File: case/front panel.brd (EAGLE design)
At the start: 165 x 30.1 mm, 3 parts, among them J16 8pin

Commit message: front panel pcb v1.0
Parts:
- added LED2: RGBLED5050, adafruit:RGBLED5050
- added R2, R3, R4: 3.3k, FlashPCB_Resistors:RES-0402
- moved LED1 1.00 mm to (73.0, 4.00)
- moved R1 1.00 mm to (71.9, 3.70)
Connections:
- new net BLUE: J16.8, R2.P$2
- new net BLUE_R: LED2.3, R2.P$1
- new net GREEN: J16.6, R3.P$2
- new net GREEN_R: LED2.1, R3.P$1
- new net RED: J16.4, R4.P$2
- new net RED_R: LED2.2, R4.P$1
- net 5V: now also J16.3, J16.5, J16.7
- net GND: now also LED2.4, LED2.5, LED2.6
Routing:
- net RED: track 0.00 -> 59.1 mm
- net BLUE: track 0.00 -> 54.1 mm
- net GND: track 0.00 -> 50.2 mm
- net GREEN: track 0.00 -> 47.6 mm
- net 5V: track 0.00 -> 23.0 mm
- net RED_R: track 0.00 -> 2.30 mm
- net GREEN_R: track 0.00 -> 2.30 mm
- net BLUE_R: track 0.00 -> 2.30 mm
- net N$1: track 0.00 -> 1.33 mm
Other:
- board text added: "HaasoscopePro v1.0 by DrAndyHaas"
- board text removed: "Haasoscope Pro Power board, v1.2 by Dr. Andy Haas"
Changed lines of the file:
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@@
 <wire x1="161" y1="30.13" x2="4" y2="30.13" width="0" layer="20"/>
 <wire x1="4" y1="30.13" x2="0" y2="26.13" width="0" layer="20" curve="90"/>
-<text x="78.277" y="20.021" size="1.4224" layer="21" font="vector">Haasoscope Pro
-Power board, v1.2
-by Dr. Andy Haas</text>
+<text x="78.277" y="20.021" size="1.778" layer="21" font="vector" ratio="10">HaasoscopePro v1.0
+by DrAndyHaas</text>
 <hole x="4.75" y="26.33" drill="4.5"/>
 <hole x="160.25" y="26.33" drill="4.5"/>
 <hole x="160.25" y="3.8" drill="4.5"/>
 <hole x="4.75" y="3.8" drill="4.5"/>
-<text x="73.428" y="5.711" size="0.8128" layer="21">5V</text>
+<text x="72.428" y="5.711" size="0.8128" layer="21">5V</text>
 <wire x1="108" y1="13" x2="120" y2="13" width="0.1524" layer="20"/>
 <wire x1="120" y1="13" x2="120" y2="8" width="0.1524" layer="20"/>
@@
 <attribute name="PROD_ID" value="CONN-08438" x="77" y="4" size="1.778" layer="27" display="off"/>
 </element>
-<element name="R1" library="FlashPCB_Resistors" package="RES-0402" value="3.3k" x="72.9" y="3.7" smashed="yes" rot="R90"/>
-<element name="LED1" library="adafruit" library_urn="urn:adsk.eagle:library:420" package="CHIP-LED0603" package3d_urn="urn:adsk.eagle:package:6240556/1" value="red" x="74" y="4" smashed="yes"/>
+<element name="R1" library="FlashPCB_Resistors" package="RES-0402" value="3.3k" x="71.9" y="3.7" smashed="yes" rot="R90"/>
+<element name="LED1" library="adafruit" library_urn="urn:adsk.eagle:library:420" package="CHIP-LED0603" package3d_urn="urn:adsk.eagle:package:6240556/1" value="red" x="73" y="4" smashed="yes"/>
+<element name="LED2" library="adafruit" library_urn="urn:adsk.eagle:library:420" package="RGBLED5050" package3d_urn="urn:adsk.eagle:package:6240865/1" value="RGBLED5050" x="39" y="11" smashed="yes" rot="R180">
+<attribute name="LCSC" value="C2827258" x="39" y="11" size="1.778" layer="27" rot="R180" display="off"/>
+<attribute name="NAME" x="40.7" y="8.1" size="1.27" layer="25" font="vector" rot="R180"/>
+</element>
+<element name="R2" library="FlashPCB_Resistors" package="RES-0402" value="3.3k" x="43.8" y="12.7" smashed="yes"/>
+<element name="R3" library="FlashPCB_Resistors" package="RES-0402" value="3.3k" x="43.8" y="9.3" smashed="yes"/>
+<element name="R4" library="FlashPCB_Resistors" package="RES-0402" value="3.3k" x="43.8" y="11" smashed="yes"/>
 </elements>
 <signals>
@@
 <contactref element="R1" pad="P$1"/>
 <contactref element="J16" pad="2"/>
-<wire x1="79.54" y1="4" x2="72.9" y2="3.2" width="0" layer="19" extent="1-1"/>
+<contactref element="LED2" pad="5"/>
+<contactref element="LED2" pad="4"/>
+<contactref element="LED2" pad="6"/>
+<wire x1="72.2952" y1="2.72375" x2="72.47375" y2="2.5452" width="0.3048" layer="1"/>
+<wire x1="71.9" y1="3.2" x2="72.2952" y2="2.8048" width="0.3048" layer="1"/>
+<wire x1="72.2952" y1="2.8048" x2="72.2952" y2="2.72375" width="0.3048" layer="1"/>
+<wire x1="72.47375" y1="2.5452" x2="78.0852" y2="2.5452" width="0.3048" layer="1"/>
+<wire x1="78.0852" y1="2.5452" x2="79.54" y2="4" width="0.3048" layer="1"/>
+<wire x1="37" y1="12.7" x2="37" y2="11" width="0.3048" layer="1"/>
+<wire x1="37" y1="11" x2="37" y2="9.3" width="0.3048" layer="1"/>
+<wire x1="37" y1="9.3" x2="43.7548" y2="2.5452" width="0.3048" layer="1"/>
+<wire x1="43.7548" y1="2.5452" x2="72.47375" y2="2.5452" width="0.3048" layer="1"/>
 </signal>
 <signal name="SW4">
@@
 <contactref element="R1" pad="P$2"/>
 <contactref element="LED1" pad="C"/>
-<wire x1="74" y1="4.75" x2="72.9" y2="4.2" width="0" layer="19" extent="1-1"/>
+<wire x1="73" y1="4.75" x2="72.45" y2="4.2" width="0.3048" layer="1"/>
+<wire x1="72.45" y1="4.2" x2="71.9" y2="4.2" width="0.3048" layer="1"/>
 </signal>
 <signal name="5V">
 <contactref element="LED1" pad="A"/>
 <contactref element="J16" pad="1"/>
-<wire x1="74" y1="3.25" x2="77" y2="4" width="0" layer="19" extent="1-1"/>
+<contactref element="J16" pad="3"/>
+<contactref element="J16" pad="5"/>
+<contactref element="J16" pad="7"/>
+<wire x1="77" y1="4" x2="76.25" y2="3.25" width="0.3048" layer="1"/>
+<wire x1="76.25" y1="3.25" x2="73" y2="3.25" width="0.3048" layer="1"/>
+<wire x1="79.02446875" y1="5.2446" x2="80.05553125" y2="5.2446" width="0.3048" layer="1"/>
+<wire x1="77" y1="4" x2="77.77986875" y2="4" width="0.3048" layer="1"/>
+<wire x1="81.30013125" y1="4" x2="82.08" y2="4" width="0.3048" layer="1"/>
+<wire x1="77.77986875" y1="4" x2="79.02446875" y2="5.2446" width="0.3048" layer="1"/>
+<wire x1="80.05553125" y1="5.2446" x2="81.30013125" y2="4" width="0.3048" layer="1"/>
+<wire x1="84.10446875" y1="2.7554" x2="85.13553125" y2="2.7554" width="0.3048" layer="1"/>
+<wire x1="82.08" y1="4" x2="82.85986875" y2="4" width="0.3048" layer="1"/>
+<wire x1="86.38013125" y1="4" x2="87.16" y2="4" width="0.3048" layer="1"/>
+<wire x1="82.85986875" y1="4" x2="84.10446875" y2="2.7554" width="0.3048" layer="1"/>
+<wire x1="85.13553125" y1="2.7554" x2="86.38013125" y2="4" width="0.3048" layer="1"/>
+<wire x1="88.9950875" y1="2.2982" x2="90.4049125" y2="2.2982" width="0.3048" layer="1"/>
+<wire x1="87.16" y1="4" x2="87.2932875" y2="4" width="0.3048" layer="1"/>
+<wire x1="92.1067125" y1="4" x2="92.24" y2="4" width="0.3048" layer="1"/>
+<wire x1="87.2932875" y1="4" x2="88.9950875" y2="2.2982" width="0.3048" layer="1"/>
+<wire x1="90.4049125" y1="2.2982" x2="92.1067125" y2="4" width="0.3048" layer="1"/>
+</signal>
+<signal name="BLUE">
+<contactref element="J16" pad="8"/>
+<contactref element="R2" pad="P$2"/>
+<wire x1="44.3" y1="12.7" x2="86.08" y2="12.7" width="0.3048" layer="1"/>
+<wire x1="86.08" y1="12.7" x2="94.78" y2="4" width="0.3048" layer="1"/>
+</signal>
+<signal name="GREEN">
+<contactref element="J16" pad="6"/>
+<contactref element="R3" pad="P$2"/>
+<wire x1="89.7" y1="4" x2="84.4" y2="9.3" width="0.3048" layer="1"/>
+<wire x1="84.4" y1="9.3" x2="44.3" y2="9.3" width="0.3048" layer="1"/>
+</signal>
+<signal name="RED">
+<contactref element="J16" pad="4"/>
+<contactref element="R4" pad="P$2"/>
+<wire x1="88.4554" y1="3.48446875" x2="89.18446875" y2="2.7554" width="0.3048" layer="1"/>
+<wire x1="89.18446875" y1="2.7554" x2="90.21553125" y2="2.7554" width="0.3048" layer="1"/>
+<wire x1="90.21553125" y1="2.7554" x2="90.9446" y2="3.48446875" width="0.3048" layer="1"/>
+<wire x1="90.9446" y1="3.48446875" x2="90.9446" y2="4.51553125" width="0.3048" layer="1"/>
+<wire x1="90.9446" y1="4.51553125" x2="90.21553125" y2="5.2446" width="0.3048" layer="1"/>
+<wire x1="84.62" y1="4" x2="85.8646" y2="5.2446" width="0.3048" layer="1"/>
+<wire x1="85.8646" y1="5.2446" x2="87.67553125" y2="5.2446" width="0.3048" layer="1"/>
+<wire x1="87.67553125" y1="5.2446" x2="88.4554" y2="4.46473125" width="0.3048" layer="1"/>
+<wire x1="88.4554" y1="4.46473125" x2="88.4554" y2="3.48446875" width="0.3048" layer="1"/>
+<wire x1="90.21553125" y1="5.2446" x2="89.7554" y2="5.2446" width="0.3048" layer="1"/>
+<wire x1="89.7554" y1="5.2446" x2="84" y2="11" width="0.3048" layer="1"/>
+<wire x1="84" y1="11" x2="44.3" y2="11" width="0.3048" layer="1"/>
+</signal>
+<signal name="BLUE_R">
+<contactref element="LED2" pad="3"/>
+<contactref element="R2" pad="P$1"/>
+<wire x1="41" y1="12.7" x2="43.3" y2="12.7" width="0.3048" layer="1"/>
+</signal>
+<signal name="GREEN_R">
+<contactref element="LED2" pad="1"/>
+<contactref element="R3" pad="P$1"/>
+<wire x1="41" y1="9.3" x2="43.3" y2="9.3" width="0.3048" layer="1"/>
+</signal>
+<signal name="RED_R">
+<contactref element="LED2" pad="2"/>
+<contactref element="R4" pad="P$1"/>
+<wire x1="41" y1="11" x2="43.3" y2="11" width="0.3048" layer="1"/>
 </signal>
 </signals>

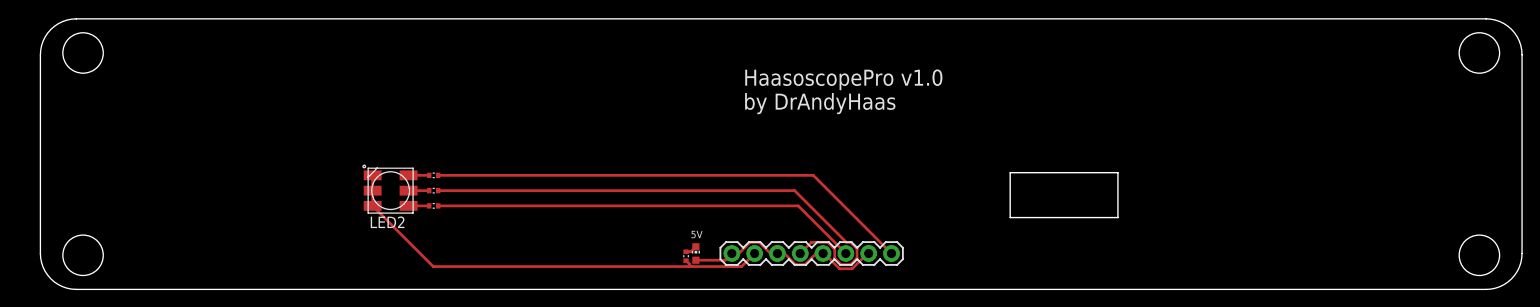
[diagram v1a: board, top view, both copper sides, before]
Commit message: did the cutouts etc
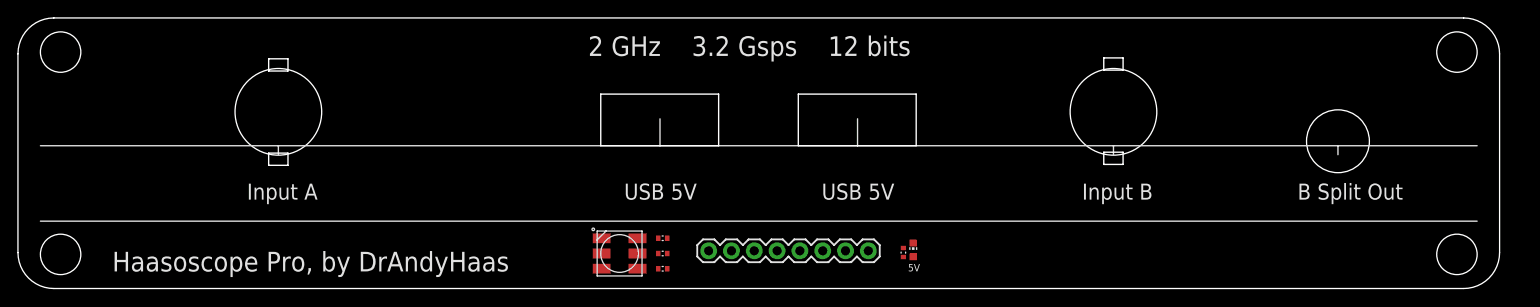
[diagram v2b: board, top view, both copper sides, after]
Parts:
- moved LED2 26.4 mm to (64.5, 4.00)
- moved R2 26.4 mm to (69.3, 5.70)
- moved R3 26.4 mm to (69.3, 2.30)
- moved R4 26.4 mm to (69.3, 4.00)
- moved LED1 24.2 mm to (97.2, 4.40)
- moved R1 24.2 mm to (96.1, 4.10)
- moved J16 15.2 mm to (92.2, 4.30), turned to 180 degrees
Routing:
- net RED: track 59.1 -> 0.00 mm
- net BLUE: track 54.1 -> 0.00 mm
- net GND: track 50.2 -> 0.00 mm
- net GREEN: track 47.6 -> 0.00 mm
- net 5V: track 23.0 -> 0.00 mm
- net RED_R: track 2.30 -> 0.00 mm
- net GREEN_R: track 2.30 -> 0.00 mm
- net BLUE_R: track 2.30 -> 0.00 mm
- net N$1: track 1.33 -> 0.00 mm
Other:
- outline, holes or cut-outs redrawn
- board text added: "2 GHz 3.2 Gsps 12 bits"
- board text added: "B Split Out"
- board text added: "Haasoscope Pro, by DrAndyHaas"
- board text added: "Input A"
- board text added: "Input B"
- board text added: "USB 5V"
- board text removed: "HaasoscopePro v1.0 by DrAndyHaas"

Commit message: move connectors a little
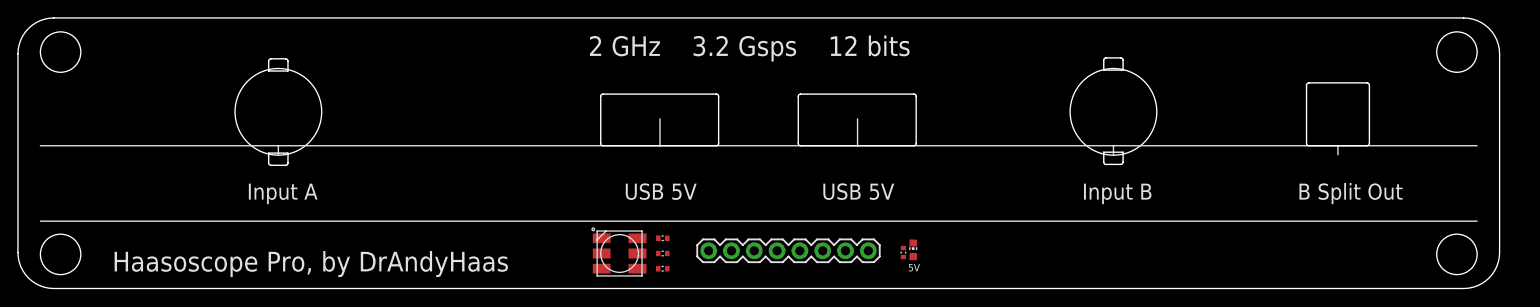
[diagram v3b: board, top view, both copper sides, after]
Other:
- outline, holes or cut-outs redrawn
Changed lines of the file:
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@@
 <drawing>
 <settings>
-<setting alwaysvectorfont="yes"/>
+<setting alwaysvectorfont="no"/>
 <setting verticaltext="up"/>
 </settings>
@@
 <hole x="2.25" y="3.9" drill="4.5"/>
 <text x="96.628" y="2.011" size="0.8128" layer="21">5V</text>
-<wire x1="84.4" y1="21.75" x2="97.53" y2="21.75" width="0.1524" layer="20"/>
-<wire x1="97.53" y1="21.75" x2="97.53" y2="16" width="0.1524" layer="20"/>
-<wire x1="97.53" y1="16" x2="84.4" y2="16" width="0.1524" layer="20"/>
-<wire x1="84.4" y1="16" x2="84.4" y2="21.75" width="0.1524" layer="20"/>
+<wire x1="84.4" y1="16.254" x2="84.4" y2="21.496" width="0.1524" layer="20"/>
+<wire x1="84.4" y1="21.496" x2="84.654" y2="21.75" width="0.1524" layer="20" curve="-90"/>
+<wire x1="84.654" y1="21.75" x2="97.276" y2="21.75" width="0.1524" layer="20"/>
+<wire x1="97.276" y1="21.75" x2="97.53" y2="21.496" width="0.1524" layer="20" curve="-90"/>
+<wire x1="97.53" y1="21.496" x2="97.53" y2="16.254" width="0.1524" layer="20"/>
+<wire x1="97.53" y1="16.254" x2="97.276" y2="16" width="0.1524" layer="20" curve="-90"/>
+<wire x1="97.276" y1="16" x2="84.654" y2="16" width="0.1524" layer="20"/>
+<wire x1="84.654" y1="16" x2="84.4" y2="16.254" width="0.1524" layer="20" curve="-90"/>
 <wire x1="26.5" y1="16" x2="26.5" y2="15" width="0.1524" layer="21"/>
 <wire x1="119.5" y1="16" x2="119.5" y2="15" width="0.1524" layer="21"/>
@@
 <wire x1="144.5" y1="16" x2="160" y2="16" width="0.1524" layer="21"/>
 <wire x1="25.42" y1="15.18" x2="27.57" y2="15.18" width="0.1524" layer="20"/>
-<wire x1="27.57" y1="15.18" x2="27.57" y2="13.82" width="0.1524" layer="20"/>
-<wire x1="27.57" y1="13.82" x2="25.42" y2="13.82" width="0.1524" layer="20"/>
-<wire x1="25.42" y1="13.82" x2="25.42" y2="15.18" width="0.1524" layer="20"/>
-<wire x1="25.42" y1="25.68" x2="27.57" y2="25.68" width="0.1524" layer="20"/>
-<wire x1="27.57" y1="25.68" x2="27.57" y2="24.32" width="0.1524" layer="20"/>
+<wire x1="27.57" y1="15.18" x2="27.57" y2="14.074" width="0.1524" layer="20"/>
+<wire x1="27.57" y1="14.074" x2="27.316" y2="13.82" width="0.1524" layer="20" curve="-90"/>
+<wire x1="27.316" y1="13.82" x2="25.674" y2="13.82" width="0.1524" layer="20"/>
+<wire x1="25.674" y1="13.82" x2="25.42" y2="14.074" width="0.1524" layer="20" curve="-90"/>
+<wire x1="25.42" y1="14.074" x2="25.42" y2="15.18" width="0.1524" layer="20"/>
+<wire x1="25.42" y1="24.32" x2="25.42" y2="25.426" width="0.1524" layer="20"/>
+<wire x1="25.42" y1="25.426" x2="25.674" y2="25.68" width="0.1524" layer="20" curve="-90"/>
+<wire x1="25.674" y1="25.68" x2="27.316" y2="25.68" width="0.1524" layer="20"/>
+<wire x1="27.316" y1="25.68" x2="27.57" y2="25.426" width="0.1524" layer="20" curve="-90"/>
+<wire x1="27.57" y1="25.426" x2="27.57" y2="24.32" width="0.1524" layer="20"/>
 <wire x1="27.57" y1="24.32" x2="25.42" y2="24.32" width="0.1524" layer="20"/>
-<wire x1="25.42" y1="24.32" x2="25.42" y2="25.68" width="0.1524" layer="20"/>
 <hole x="119.5" y="19.775" drill="9.65"/>
 <wire x1="118.42" y1="15.28" x2="120.57" y2="15.28" width="0.1524" layer="20"/>
-<wire x1="120.57" y1="15.28" x2="120.57" y2="13.92" width="0.1524" layer="20"/>
-<wire x1="120.57" y1="13.92" x2="118.42" y2="13.92" width="0.1524" layer="20"/>
-<wire x1="118.42" y1="13.92" x2="118.42" y2="15.28" width="0.1524" layer="20"/>
-<wire x1="118.42" y1="25.78" x2="120.57" y2="25.78" width="0.1524" layer="20"/>
-<wire x1="120.57" y1="25.78" x2="120.57" y2="24.42" width="0.1524" layer="20"/>
+<wire x1="120.57" y1="15.28" x2="120.57" y2="14.174" width="0.1524" layer="20"/>
+<wire x1="120.57" y1="14.174" x2="120.316" y2="13.92" width="0.1524" layer="20" curve="-90"/>
+<wire x1="120.316" y1="13.92" x2="118.674" y2="13.92" width="0.1524" layer="20"/>
+<wire x1="118.674" y1="13.92" x2="118.42" y2="14.174" width="0.1524" layer="20" curve="-90"/>
+<wire x1="118.42" y1="14.174" x2="118.42" y2="15.28" width="0.1524" layer="20"/>
+<wire x1="118.42" y1="24.42" x2="118.42" y2="25.526" width="0.1524" layer="20"/>
+<wire x1="118.42" y1="25.526" x2="118.674" y2="25.78" width="0.1524" layer="20" curve="-90"/>
+<wire x1="118.674" y1="25.78" x2="120.316" y2="25.78" width="0.1524" layer="20"/>
+<wire x1="120.316" y1="25.78" x2="120.57" y2="25.526" width="0.1524" layer="20" curve="-90"/>
+<wire x1="120.57" y1="25.526" x2="120.57" y2="24.42" width="0.1524" layer="20"/>
 <wire x1="120.57" y1="24.42" x2="118.42" y2="24.42" width="0.1524" layer="20"/>
-<wire x1="118.42" y1="24.42" x2="118.42" y2="25.78" width="0.1524" layer="20"/>
-<wire x1="62.4" y1="21.75" x2="75.53" y2="21.75" width="0.1524" layer="20"/>
-<wire x1="75.53" y1="21.75" x2="75.53" y2="16" width="0.1524" layer="20"/>
-<wire x1="75.53" y1="16" x2="62.4" y2="16" width="0.1524" layer="20"/>
-<wire x1="62.4" y1="16" x2="62.4" y2="21.75" width="0.1524" layer="20"/>
-<hole x="144.5" y="16.5" drill="7"/>
+<wire x1="75.276" y1="16" x2="62.654" y2="16" width="0.1524" layer="20"/>
+<wire x1="62.654" y1="16" x2="62.4" y2="16.254" width="0.1524" layer="20" curve="-90"/>
+<wire x1="62.4" y1="16.254" x2="62.4" y2="21.496" width="0.1524" layer="20"/>
+<wire x1="62.4" y1="21.496" x2="62.654" y2="21.75" width="0.1524" layer="20" curve="-90"/>
+<wire x1="62.654" y1="21.75" x2="75.276" y2="21.75" width="0.1524" layer="20"/>
+<wire x1="75.276" y1="21.75" x2="75.53" y2="21.496" width="0.1524" layer="20" curve="-90"/>
+<wire x1="75.53" y1="21.496" x2="75.53" y2="16.254" width="0.1524" layer="20"/>
+<wire x1="75.53" y1="16.254" x2="75.276" y2="16" width="0.1524" layer="20" curve="-90"/>
 <text x="23" y="10" size="1.778" layer="21" font="vector">Input A</text>
 <wire x1="0" y1="7.6" x2="160" y2="7.6" width="0.1524" layer="21"/>
@@
 <text x="87" y="10" size="1.778" layer="21" font="vector">USB 5V</text>
 <text x="61" y="26" size="2.1844" layer="21" font="vector">2 GHz    3.2 Gsps    12 bits</text>
+<wire x1="147.746" y1="16" x2="141.254" y2="16" width="0.1524" layer="20"/>
+<wire x1="141.254" y1="16" x2="141" y2="16.254" width="0.1524" layer="20" curve="-90"/>
+<wire x1="141" y1="16.254" x2="141" y2="22.746" width="0.1524" layer="20"/>
+<wire x1="141" y1="22.746" x2="141.254" y2="23" width="0.1524" layer="20" curve="-90"/>
+<wire x1="141.254" y1="23" x2="147.746" y2="23" width="0.1524" layer="20"/>
+<wire x1="147.746" y1="23" x2="148" y2="22.746" width="0.1524" layer="20" curve="-90"/>
+<wire x1="148" y1="22.746" x2="148" y2="16.254" width="0.1524" layer="20"/>
+<wire x1="148" y1="16.254" x2="147.746" y2="16" width="0.1524" layer="20" curve="-90"/>
 </plain>
 <attributes>
